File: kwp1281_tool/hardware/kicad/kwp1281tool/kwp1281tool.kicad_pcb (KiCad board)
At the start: 2 copper layers, 69.8 x 57.1 mm, 27 parts, among them J1 AVR-JTAG-10, J2 TTL-232R-5V, J3 Conn_01x04_Male, SW1 SW_Omron_B3FS, U1 L9637D, U2 LD1117S50CTR, U3 ATmega1284-P, U4 ISO6721BQDRQ1, Y1 18.432 MHz

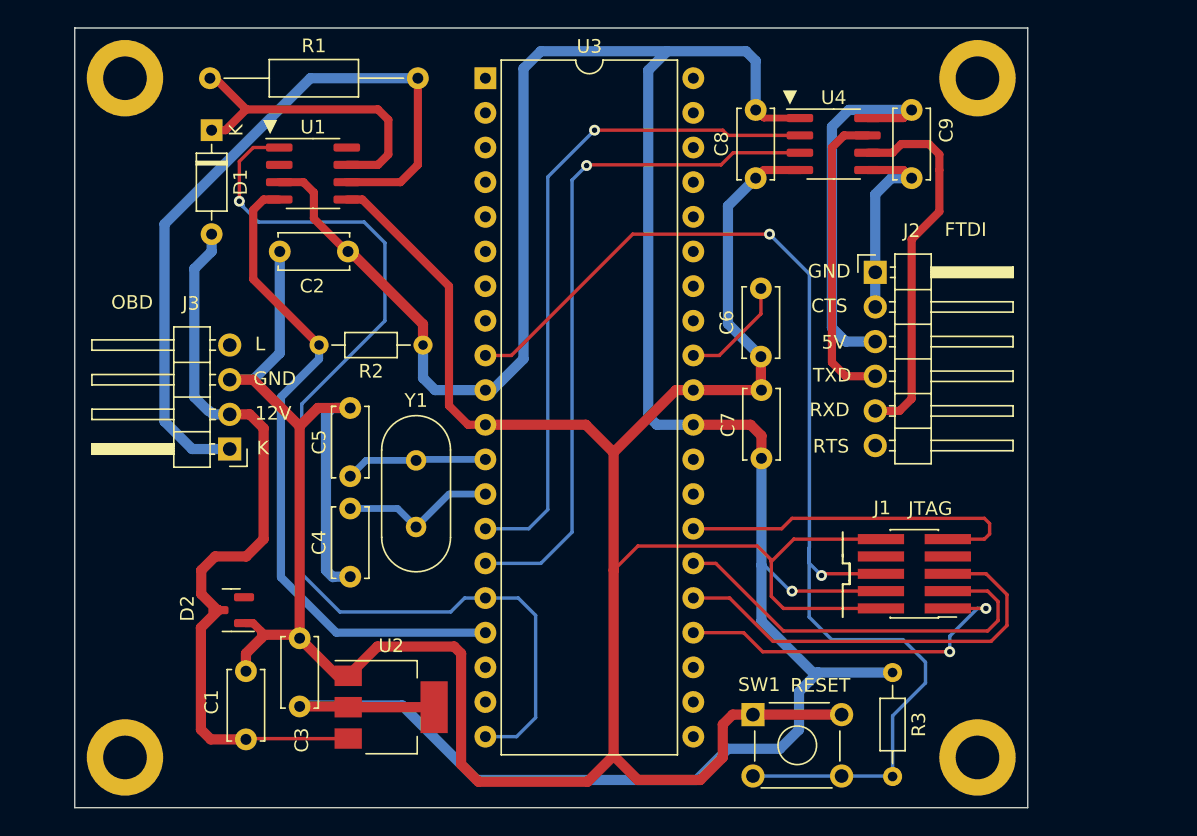
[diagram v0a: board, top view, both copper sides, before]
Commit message: Integrate USB onto the board
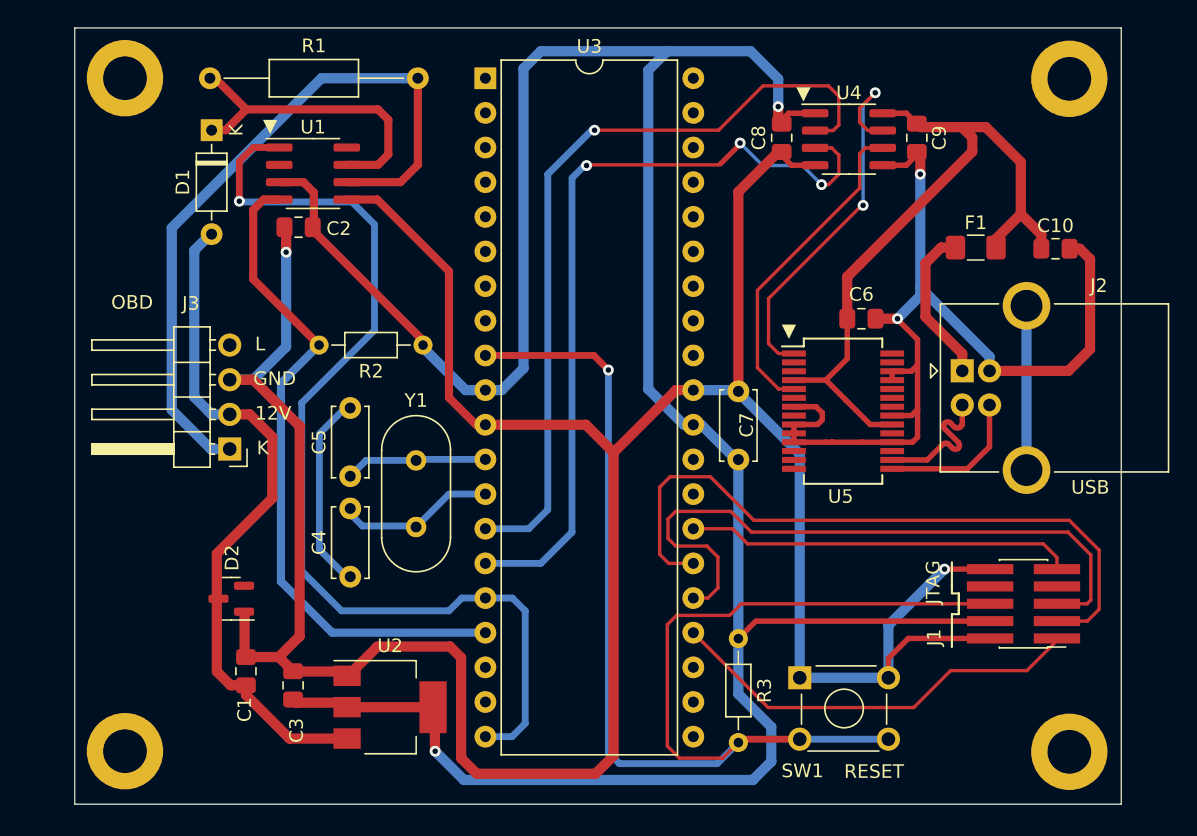
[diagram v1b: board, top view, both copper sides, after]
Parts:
- added C10: 10μF, Capacitor_SMD:C_0805_2012Metric_Pad1.18x1.45mm_HandSolder, F.Cu at (189.0, 80.0)
- added F1: 1206L150, Fuse:Fuse_1206_3216Metric_Pad1.42x1.75mm_HandSolder, F.Cu at (183.1, 79.9)
- added U5: FT232RL, Package_SO:SSOP-28_5.3x10.2mm_P0.65mm, F.Cu at (173.4, 91.9)
- C1, C2, C3, C6, C8, C9: footprint Capacitor_THT:C_Disc_D5.0mm_W2.5mm_P5.00mm -> Capacitor_SMD:C_0805_2012Metric_Pad1.18x1.45mm_HandSolder
- J2: value TTL-232R-5V -> USB_B; footprint Connector_PinHeader_2.54mm:PinHeader_1x06_P2.54mm_Horizontal -> Connector_USB:USB_B_OST_USB-B1HSxx_Horizontal
- moved R3 11.6 mm to (165.7, 108.6)
- moved J2 9.64 mm to (182.1, 89.0)
- moved J1 8.30 mm to (186.8, 106.1)
- moved C6 7.87 mm to (174.8, 85.1), turned to 180 degrees
- moved REF** 6.74 mm to (190.0, 116.9)
- moved REF** 6.73 mm to (190.0, 67.6)
- moved SW1 4.36 mm to (170.2, 111.5)
- moved C8 3.52 mm to (168.9, 71.9)
- moved C9 2.98 mm to (178.8, 71.9)
- moved C2 2.25 mm to (133.5, 78.4)
- moved C7 1.69 mm to (165.7, 90.5)
- moved C3 1.62 mm to (133.1, 112.0)
- moved U4 1.17 mm to (173.8, 72.0)
- moved D2 0.84 mm to (128.6, 105.7)
- moved REF** 0.46 mm to (120.8, 116.8)
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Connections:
- C4 pad 1: GND -> Net-(C4-Pad1)
- C5 pad 1: GND -> Net-(C4-Pad1)
- C6 pad 1: GND -> FTDI_GND
- C6 pad 2: Net-(U3-AREF) -> FTDI_VCC
- J2 pad 1: FTDI_GND -> Net-(J2-VBUS)
- J2 pad 2: FTDI_GND -> /USB_D-
- J2 pad 3: FTDI_VCC -> /USB_D+
- J2 pad 4: FTDI_TXD -> FTDI_GND
- J2 pad 5: FTDI_RXD -> unconnected-(J2-Shield-Pad5)
- U3 pad 32: Net-(U3-AREF) -> unconnected-(U3-AREF-Pad32)
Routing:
- net FTDI_GND: track 14.9 -> 73.1 mm, vias 0 -> 2
- net FTDI_VCC: track 28.2 -> 53.6 mm
- net TDO: track 30.1 -> 50.2 mm
- net GND: track 237.9 -> 218.4 mm, vias 0 -> 2
- net TMS: track 32.0 -> 48.5 mm
- net Net-(C4-Pad1): track 0.00 -> 14.6 mm
- net unconnected-(J2-Shield-Pad5): track 0.00 -> 12.0 mm
- net Net-(J2-VBUS): track 0.00 -> 11.7 mm
- net /USB_D+: track 0.00 -> 10.9 mm
- net /USB_D-: track 0.00 -> 10.8 mm
- net HOST_TX: track 50.6 -> 61.0 mm, vias 1 -> 3
- net VCC: track 200.5 -> 191.3 mm, vias 1 -> 2
- net NRST: track 90.1 -> 98.7 mm, vias 2 -> 1
- net HOST_RX: track 49.6 -> 58.1 mm
- net Net-(U3-AREF): track 8.08 -> 0.00 mm
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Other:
- board size 69.8 x 57.1 mm -> 76.7 x 56.9 mm
- board text added: "KWP1281 TOOL REV. 2 © 2023 MIKE NABEREZNY"
- board text added: "USB"
- board text removed: "5V"
- board text removed: "CTS"
- board text removed: "FTDI"
- board text removed: "KWP1281 TOOL REV. 1 © 2023 MIKE NABEREZNY"
- board text removed: "RTS"
- board text removed: "RXD"
- board text removed: "TXD"

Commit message: Add pass-through circuit
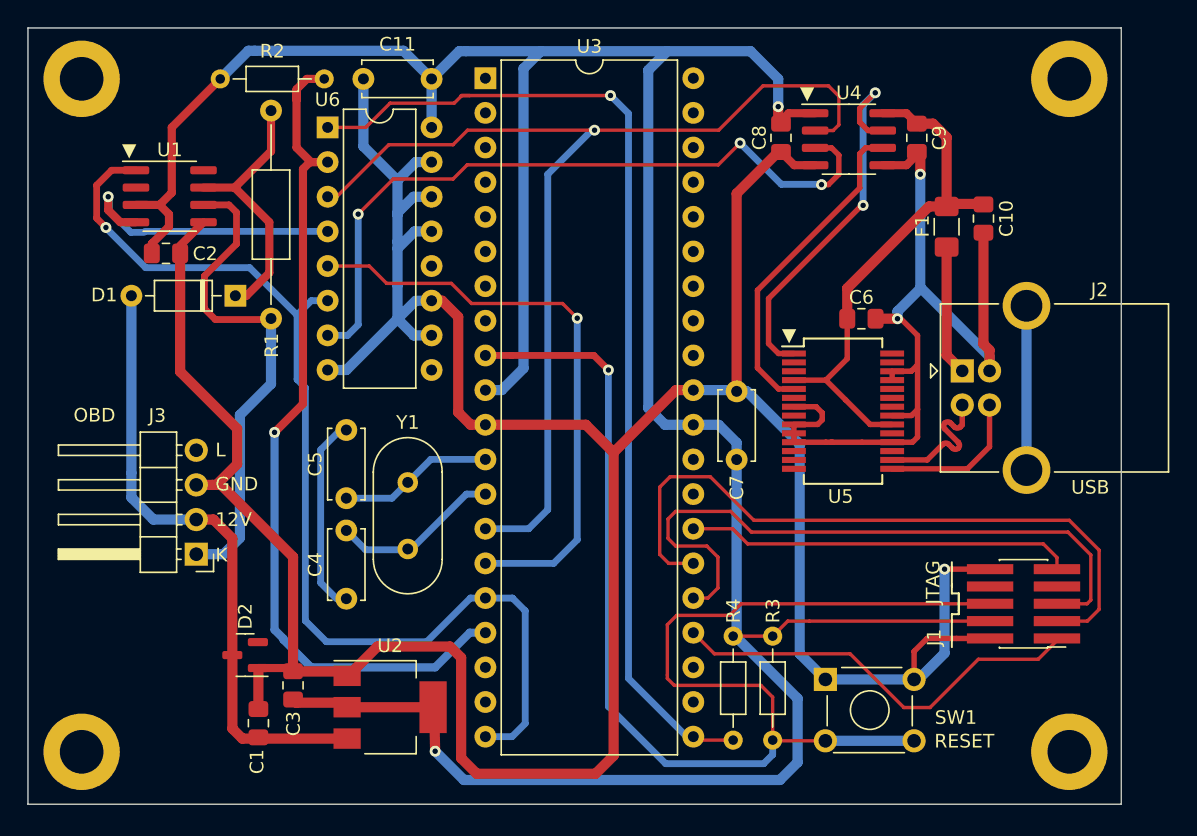
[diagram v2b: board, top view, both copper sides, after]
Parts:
- removed the REF** at (120.8, 67.5)
- removed the REF** at (120.8, 116.8)
- added C11: 0.1uF, Capacitor_THT:C_Disc_D5.0mm_W2.5mm_P5.00mm, F.Cu at (143.2, 67.6)
- added R4: 10K, Resistor_THT:R_Axial_DIN0204_L3.6mm_D1.6mm_P7.62mm_Horizontal, F.Cu at (165.4, 108.4)
- added REF**: MountingHole_3.2mm_M3_DIN965_Pad, MountingHole:MountingHole_3.2mm_M3_DIN965_Pad, F.Cu at (117.6, 67.6)
- added REF**: MountingHole_3.2mm_M3_DIN965_Pad, MountingHole:MountingHole_3.2mm_M3_DIN965_Pad, F.Cu at (117.6, 116.9)
- added U6: 74LS257, Package_DIP:DIP-16_W7.62mm, F.Cu at (135.6, 71.1)
- moved R2 24.5 mm to (127.8, 67.6), turned to 0 degrees
- moved D1 12.3 mm to (128.9, 83.5), turned to 180 degrees
- moved U1 10.6 mm to (124.1, 76.2)
- moved C2 9.91 mm to (123.8, 80.4), turned to 180 degrees
- moved J3 8.09 mm to (126.0, 102.4)
- moved C10 5.72 mm to (183.7, 77.8), turned to -90 degrees
- moved R1 5.07 mm to (131.5, 69.9), turned to -90 degrees
- moved D2 4.25 mm to (129.6, 109.8)
- moved C1 3.92 mm to (130.6, 114.8)
- moved F1 2.62 mm to (181.0, 78.4), turned to 90 degrees
- moved R3 2.52 mm to (168.2, 108.4)
- moved SW1 1.88 mm to (172.1, 111.6)
- moved Y1 1.72 mm to (141.5, 102.0)
- moved C4 1.64 mm to (137.0, 105.7)
- moved C5 1.64 mm to (137.0, 93.3)
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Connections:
- net HOST_RX renamed AVR_CTRL_RX
- C8 pad 1: GND -> VCC
- C8 pad 2: VCC -> GND
- R2 pad 2: L9637D_TX -> AVR_KLINE_TX
- U3 pad 15: HOST_TX -> AVR_CTRL_TX
- U3 pad 17: L9637D_TX -> AVR_KLINE_TX
- U3 pad 21: unconnected-(U3-PD7-Pad21) -> PASSTHRU
- U4 pad 3: HOST_TX -> ISO_RX
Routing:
- net PASSTHRU: track 0.00 -> 75.1 mm, vias 0 -> 1
- net AVR_KLINE_TX: track 0.00 -> 64.3 mm, vias 0 -> 1
- net HOST_TX: track 61.0 -> 0.00 mm, vias 3 -> 0
- net ISO_RX: track 0.00 -> 53.0 mm, vias 0 -> 3
- net AVR_CTRL_TX: track 0.00 -> 43.7 mm, vias 0 -> 1
- net GND: track 218.4 -> 247.8 mm, vias 2 -> 1
- net L9637D_TX: track 49.2 -> 21.1 mm, vias 0 -> 1
- net VCC: track 191.3 -> 219.2 mm
- net AVR_CTRL_RX: track 58.1 -> 79.7 mm
- net K_LINE: track 53.4 -> 36.5 mm
- net FTDI_VCC: track 53.6 -> 39.3 mm
- net FTDI_GND: track 73.1 -> 67.1 mm
- net 12V: track 50.5 -> 46.2 mm
- net L9637D_RX: track 74.4 -> 78.6 mm
- net Net-(D1-K): track 23.4 -> 19.5 mm
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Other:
- board size 76.7 x 56.9 mm -> 80.1 x 56.9 mm
- board text added: "D+"
- board text added: "D-"
- board text added: "KWP1281 TOOL REV. 3 © 2023 MIKE NABEREZNY"
- board text added: "VBUS"
- board text removed: "KWP1281 TOOL REV. 2 © 2023 MIKE NABEREZNY"
